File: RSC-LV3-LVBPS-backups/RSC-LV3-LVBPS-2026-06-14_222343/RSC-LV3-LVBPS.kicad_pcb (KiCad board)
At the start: 2 copper layers, 210 x 60 mm, 122 parts, among them J1 Conn_01x02, J2 Molex 43045-0400, J3 Conn_01x02, J4 Conn_01x02, J5 FTSH-105-01-L-DV-K-A, J6 USB_C_Receptacle_USB2.0_16P, J7 Molex 43650-0500, J8 Molex 43650-0500, K1 SANYOU_SRD_Form_A, K2 SANYOU_SRD_Form_A, Q1 AO3400A, Q2 AO3400A, Q3 AO3400A, U1 INA181A2, U2 INA181A2, U3 STM32G0B1CBTx, U4 TPS54302, U5 TLV74033PDBVR, U6 TLP175A, U7 TJA1051T-3, Y1 32.768 kHz 6pF, Y2 Crystal_GND24

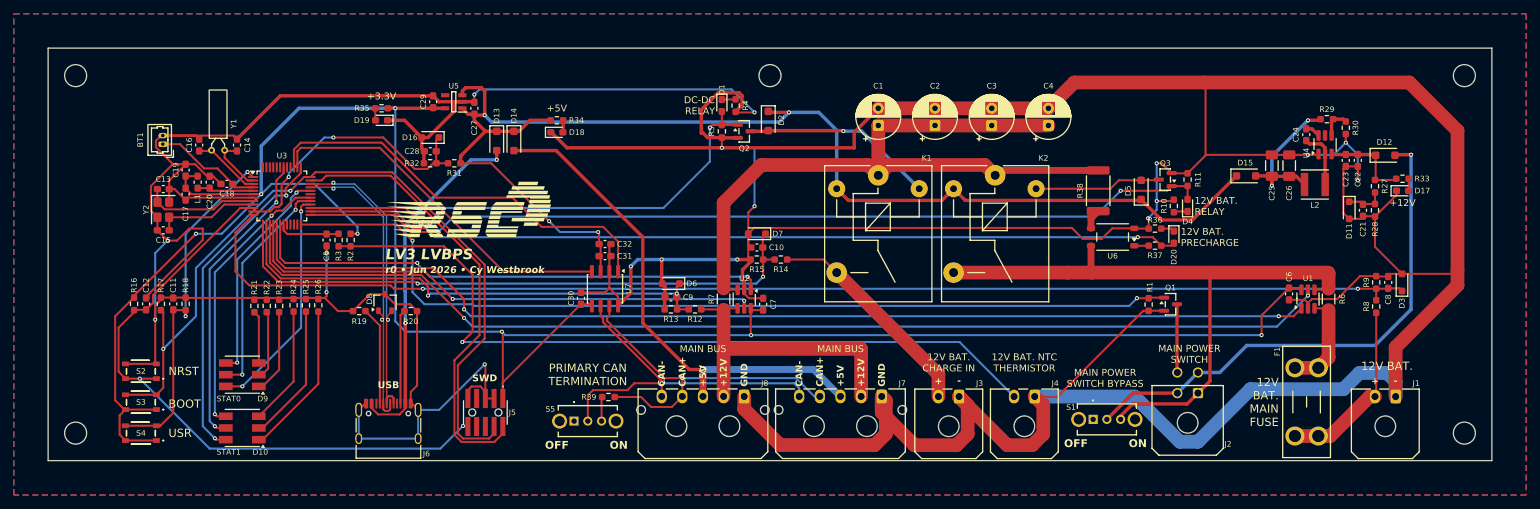
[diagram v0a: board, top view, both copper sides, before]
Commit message: finished layout, routing, and silkscreen
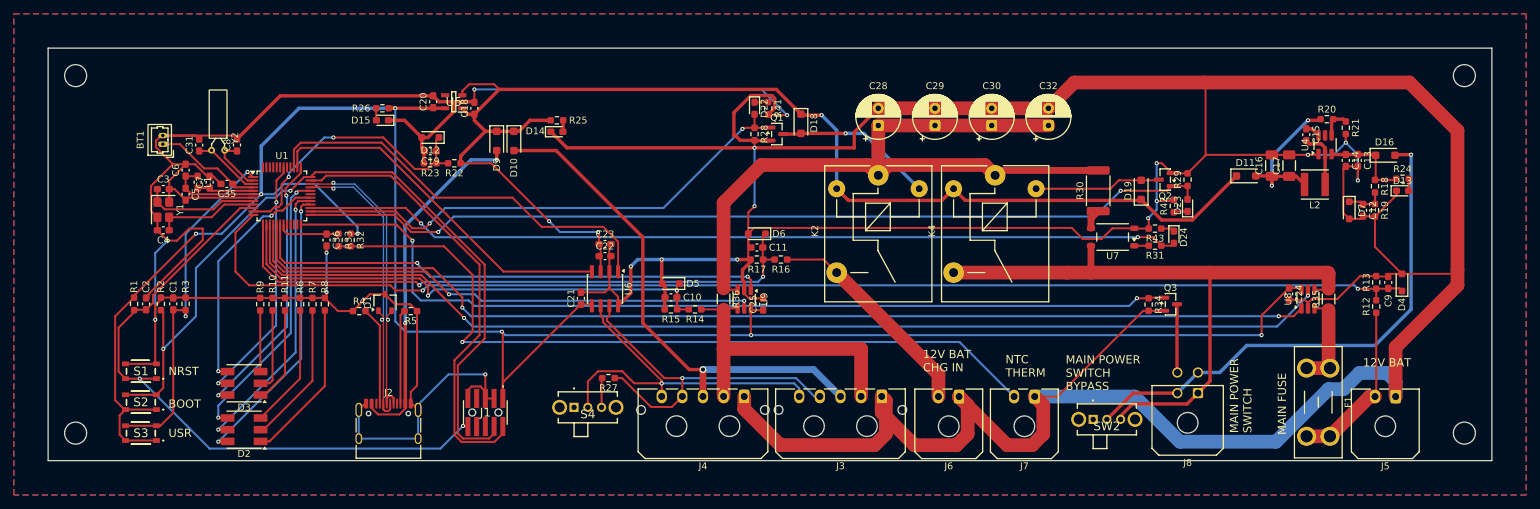
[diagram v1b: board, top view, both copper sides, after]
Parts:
- moved D2 8.00 mm to (78.5, 105.5)
- moved R6 6.65 mm to (86.7, 87.2)
- moved R7 6.65 mm to (88.5, 87.2)
- moved R8 6.65 mm to (90.2, 87.2)
- moved D3 6.50 mm to (78.5, 98.8)
- moved R9 4.85 mm to (80.8, 87.2)
- moved R10 4.85 mm to (82.7, 87.2)
- moved R11 4.85 mm to (84.5, 87.2)
- moved D18 4.77 mm to (159.5, 61.0)
- moved D22 4.77 mm to (152.8, 58.8)
- moved Q1 4.77 mm to (156.0, 62.5)
- moved R28 4.77 mm to (152.8, 62.5)
- moved R41 4.77 mm to (154.8, 58.8)
- moved R27 2.75 mm to (131.5, 98.0)
- moved S4 2.00 mm to (126.5, 102.2)
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- renumbered C11 to C1, C9 to C10, C10 to C11, C21 to C12, C22 to C13, C23 to C14, C24 to C15, C25 to C16, C26 to C17, C27 to C18, C28 to C19, C12 to C2, C29 to C20, C30 to C21, C31 to C22, C32 to C23, C6 to C24, C7 to C25, C1 to C28, C2 to C29, C13 to C3, C3 to C30, C16 to C31, C4 to C32, C18 to C35, C5 to C36, C15 to C4, C17 to C5, C19 to C6, C20 to C7, C14 to C8, C8 to C9, D8 to D1, D14 to D10, D15 to D11, D16 to D12, D17 to D13, D18 to D14, D19 to D15, D12 to D16, D2 to D18, D5 to D19, D9 to D2, D1 to D22, D4 to D23, D20 to D24, D10 to D3, D3 to D4, D6 to D5, D7 to D6, D11 to D7, D13 to D9, J5 to J1, J6 to J2, J7 to J3, J8 to J4, J1 to J5, J3 to J6, J4 to J7, J2 to J8, K1 to K2, K2 to K4, Q2 to Q1, Q3 to Q2, Q1 to Q3, R16 to R1, R25 to R10, R26 to R11, R8 to R12, R9 to R13, R12 to R14, R13 to R15, R14 to R16, R15 to R17, R27 to R18, R28 to R19, R17 to R2, R29 to R20, R30 to R21, R31 to R22, R32 to R23, R33 to R24, R34 to R25, R35 to R26, R39 to R27, R5 to R28, R11 to R29, R18 to R3, R38 to R30, R37 to R31, R2 to R32, R3 to R33, R1 to R34, R6 to R35, R7 to R36, R19 to R4, R4 to R41, R10 to R42, R36 to R43, R20 to R5, R21 to R6, R22 to R7, R23 to R8, R24 to R9, S2 to S1, S3 to S2, S4 to S3, S5 to S4, S1 to SW2, U3 to U1, U7 to U6, U6 to U7, U1 to U8, U2 to U9, Y2 to Y1, Y1 to Y2
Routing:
- net Net-(D2-RK): track 12.3 -> 23.7 mm
- net Net-(D2-GK): track 9.99 -> 20.7 mm
- net Net-(D2-BK): track 7.66 -> 18.0 mm
- net STAT1_R: track 48.7 -> 39.7 mm
- net STAT0_B: track 32.1 -> 41.0 mm
- net STAT0_R: track 33.6 -> 42.0 mm
- net Net-(D3-RK): track 22.5 -> 14.1 mm
- net Net-(D3-BK): track 17.3 -> 8.91 mm
- net STAT0_G: track 32.8 -> 41.2 mm
- net Net-(D3-GK): track 20.1 -> 12.1 mm
- net STAT1_G: track 44.1 -> 36.7 mm
- net STAT1_B: track 40.8 -> 34.6 mm
- net Net-(D18-A): track 28.1 -> 23.1 mm
- net GND: track 936.8 -> 940.2 mm
- net +5V: track 190.1 -> 187.8 mm, vias 4 -> 3
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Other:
- outline, holes or cut-outs redrawn
- board text added: "12V BAT"
- board text added: "12V BAT CHG IN"
- board text added: "MAIN FUSE"
- board text added: "NTC THERM"
- board text removed: "+"
- board text removed: "+12V"
- board text removed: "+3.3V"
- board text removed: "+5V"
- board text removed: "-"
- board text removed: "12V BAT."
- board text removed: "12V BAT. CHARGE IN"
- board text removed: "12V BAT. MAIN FUSE"
- board text removed: "12V BAT. NTC THERMISTOR"
- board text removed: "12V BAT. PRECHARGE"
- board text removed: "12V BAT. RELAY"
- board text removed: "CAN+"
- board text removed: "CAN-"
- board text removed: "DC-DC RELAY"
- board text removed: "GND"
- board text removed: "LED+"
- board text removed: "LED-"
- board text removed: "LV3 LVBPS"
- board text removed: "MAIN BUS"
- board text removed: "OFF"
- board text removed: "ON"
- board text removed: "PRIMARY CAN TERMINATION"
- board text removed: "STAT0"
- board text removed: "STAT1"
- board text removed: "SW"
- board text removed: "SWD"
- board text removed: "USB"
- board text removed: "r0 • Jun 2026 • Cy Westbrook"
